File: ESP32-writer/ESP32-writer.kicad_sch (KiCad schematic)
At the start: 27 parts, among them J1 USB2.0_C, J2 USB2.0_C, J3 ESP-Prog-ProgramCOM-SEND, J4 UART-OUTPUT, Q1 2N7002, Q2 2N7002, U1 AMS1117-3.3, U2 CH340G, Y1 12M

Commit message: type ch340g
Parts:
- removed C3, C5: 22p, $74th:Capacitor_0805_2012, symbol Device:C
- removed C6: 1u, $74th:Capacitor_0805_2012, symbol Device:C
- removed C7: 100n, $74th:Capacitor_0805_2012, symbol Device:C
- removed F1, F2: Polyfuse, $74th:ResettableFuse_KT6-1100SMDI, symbol Device:Polyfuse
- removed JP1: Jumper_3_Open, Jumper:SolderJumper-3_P1.3mm_Open_RoundedPad1.0x1.5mm_NumberLabels, symbol Jumper:Jumper_3_Open
- removed JP2: Jumper_2_Open, Jumper:SolderJumper-2_P1.3mm_Open_RoundedPad1.0x1.5mm, symbol Jumper:Jumper_2_Open
- removed U1: AMS1117-3.3, Package_TO_SOT_SMD:SOT-223-3_TabPin2, symbol Regulator_Linear:AMS1117-3.3
- removed Y1: 12M, $74th:Crystal_SMD_3225-4Pin_3.2x2.5mm_HandSoldering, symbol Device:Crystal_GND24
- added C4: 10u, $74th:Capacitor_0805_2012, symbol Device:C
- C1: value 1u -> 10u
- C3: renamed from C4; value 1u -> 100n
- J1: footprint $74th:USB-C-12-Pin-MidMount-ali-v5 -> $74th:USB-C-12-Pin-MidMount-ali-v4
- J2: renamed from J4; symbol esp32-dev-board:UART-OUTPUT-v2 -> esp32-dev-board:UART-OUTPUT
- J3: renamed from J2; footprint $74th:USB-C-12-Pin-MidMount-ali-v5 -> $74th:USB-C-12-Pin-MidMount-ali-v4
- R3: renamed from R1; value 200 -> 1k
- U1: renamed from U2; value CH340G -> CH340C; symbol $74th:CH340G -> esp32-dev-board:CH340C
- renumbered D2 to D1, D1 to D2, Q2 to Q1, Q1 to Q2, R4 to R1, R5 to R2, R2 to R4, R3 to R5, J3 to U2
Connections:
- net +3V3 is gone; now on net GND: J2.4 (GND)
- net +5V: now also J1.1 (VBUS), C4.1
- net BOOT: now also J2.6 (BOOT); no longer J2.7 (BOOT)
- net GND: now also C4.2; no longer J2.5 (GND)
- net RESET: now also J2.5 (EN); no longer J2.6 (EN)
- net at D2.2 (A): now also J3.1 (VBUS)
- net +3.3V: now reaches U1.4 (V3)
- net +3.3V: now also C2.1
- no-connect marks 6 -> 8
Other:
- moved on the sheet: C1, C2, C3, D1, D2, J1, J3, Q1, Q2, R1, R2, R3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

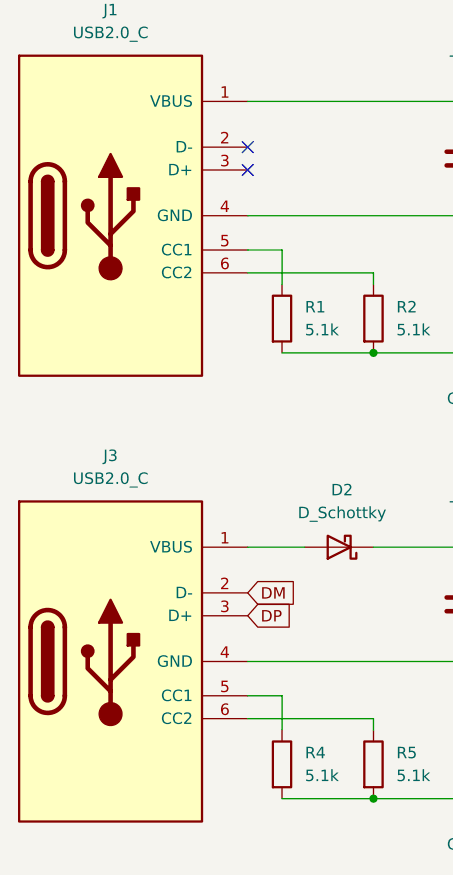
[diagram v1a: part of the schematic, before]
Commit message: replace usb type-c
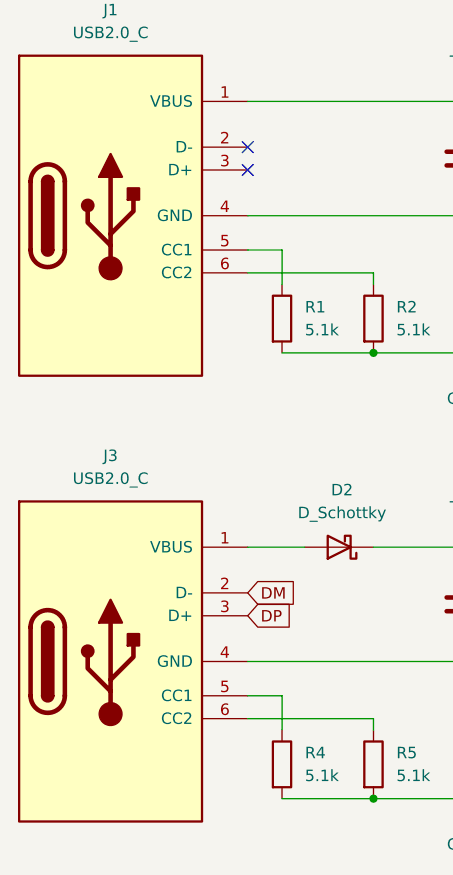
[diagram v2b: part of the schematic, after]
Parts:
- J1, J3: footprint $74th:USB-C-12-Pin-MidMount-ali-v4 -> $74th:USB-C-12-Pin-MidMount-ali-v5
